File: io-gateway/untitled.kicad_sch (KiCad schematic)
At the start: 6 parts, among them J1 1752201, J2 1752201, J3 1752201, J4 Screw_Terminal_01x09, J5 Screw_Terminal_01x09, J6 Screw_Terminal_01x09

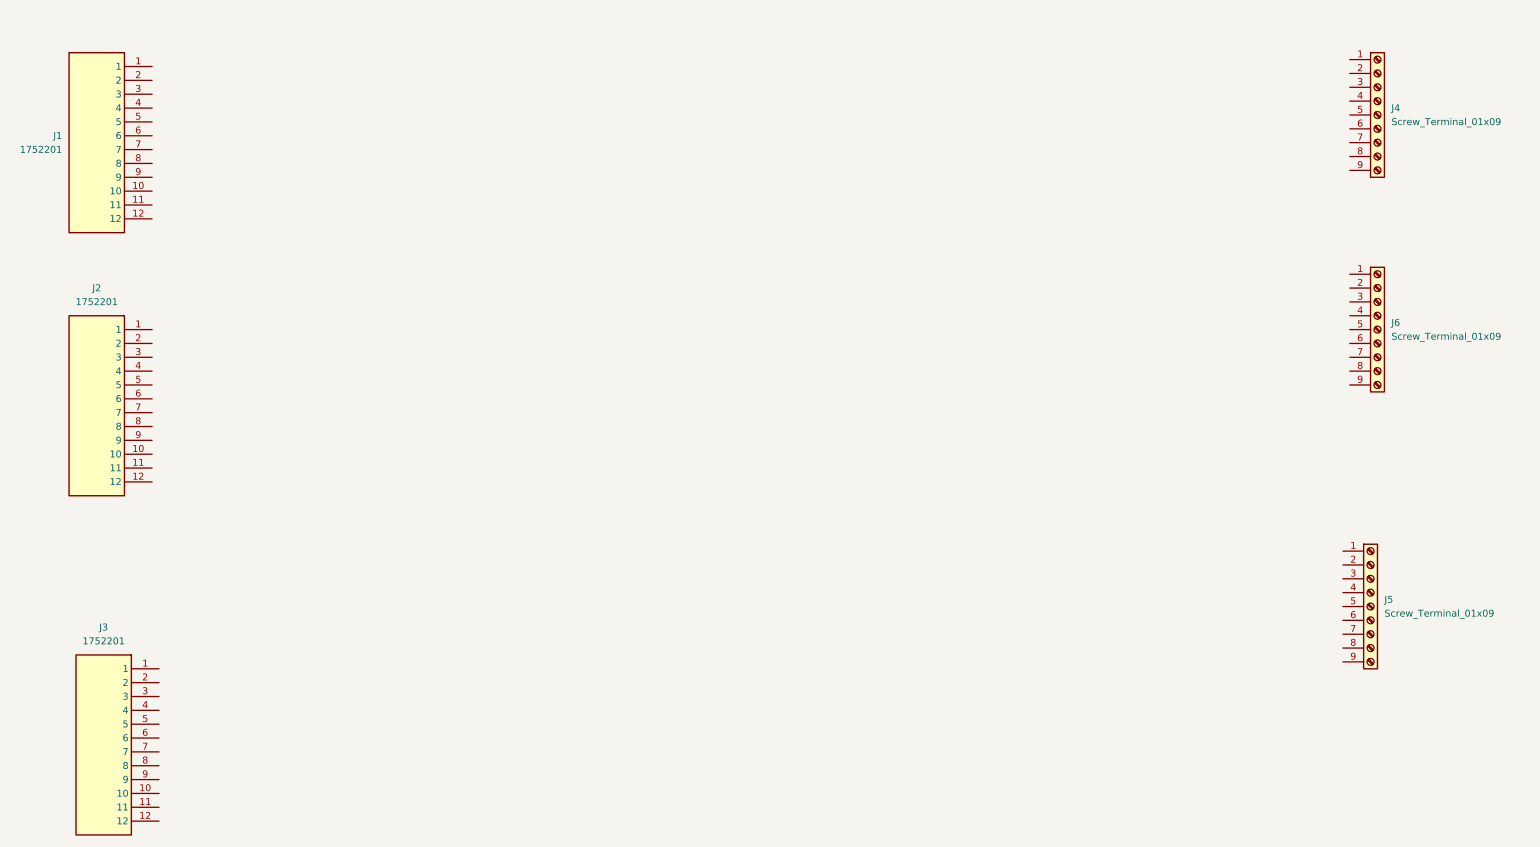
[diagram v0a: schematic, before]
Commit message: Label Terminal Block Pins
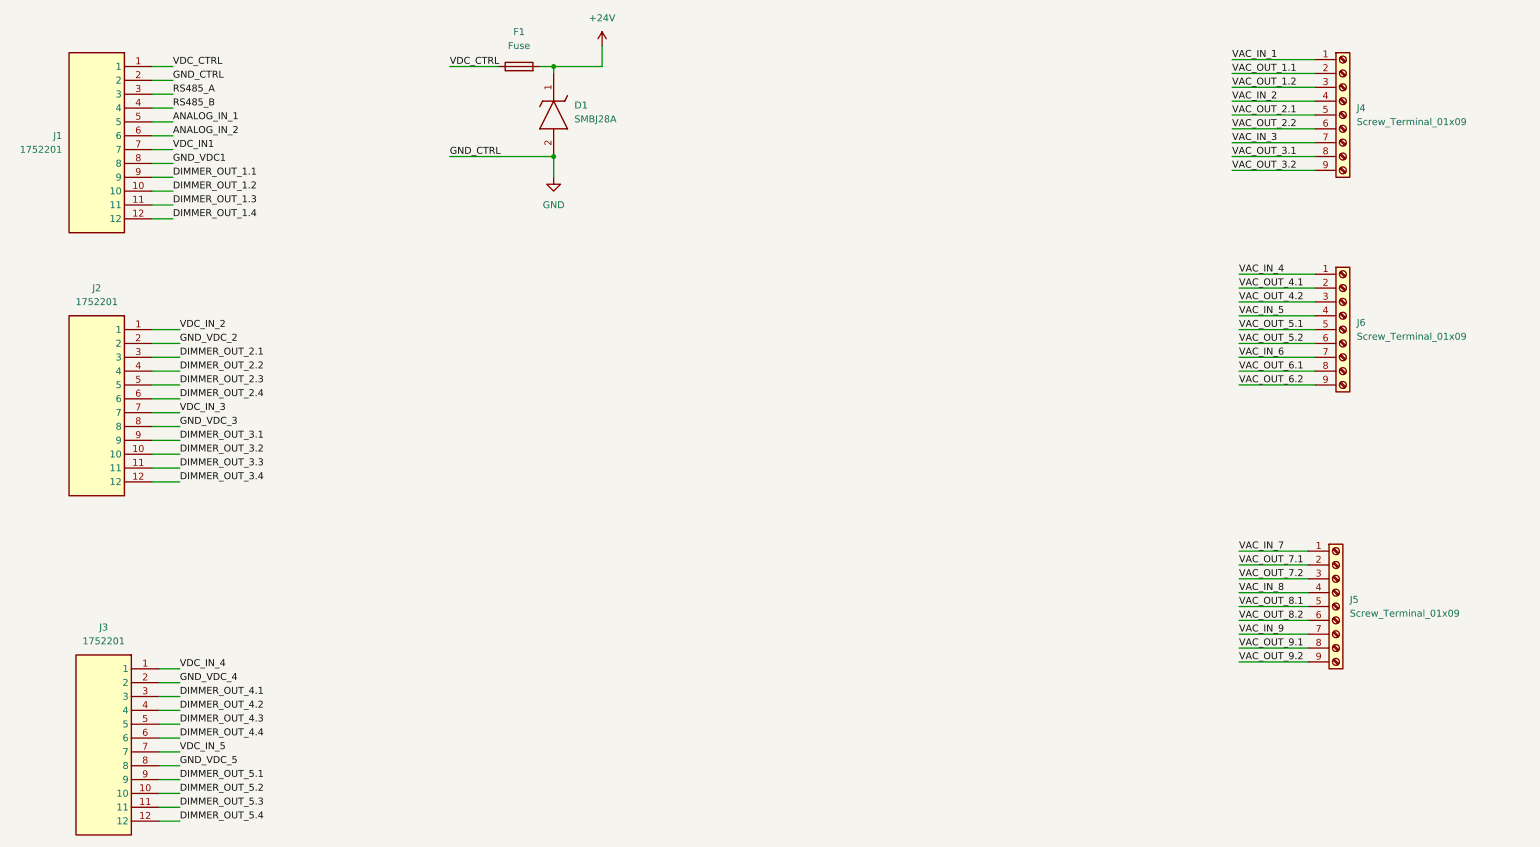
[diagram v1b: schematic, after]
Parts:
- added D1: SMBJ28A, TVS_Diodes:DIOM5436X244N, symbol SMBJ28A:SMBJ28A
- added F1: Fuse, Fuse:Fuseholder_Cylinder-5x20mm_Wuerth_696103101002-SMD_Horizontal_Open, symbol Device:Fuse
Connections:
- net VDC_CTRL: now reaches J1.1
- net VDC_CTRL: now also F1.1
- net DIMMER_OUT_1.2: now reaches J1.10
- net DIMMER_OUT_1.3: now reaches J1.11
- net DIMMER_OUT_1.4: now reaches J1.12
- net GND: now reaches J1.2
- net GND: now also D1.2 (A)
- net RS485_A: now reaches J1.3
- net RS485_B: now reaches J1.4
- net ANALOG_IN_1: now reaches J1.5
- net ANALOG_IN_2: now reaches J1.6
- net VDC_IN1: now reaches J1.7
- net GND_VDC1: now reaches J1.8
- net DIMMER_OUT_1.1: now reaches J1.9
- net VDC_IN_4: now reaches J3.1
- net DIMMER_OUT_5.2: now reaches J3.10
- net DIMMER_OUT_5.3: now reaches J3.11
- net DIMMER_OUT_5.4: now reaches J3.12
- net GND_VDC_4: now reaches J3.2
- net DIMMER_OUT_4.1: now reaches J3.3
- net DIMMER_OUT_4.2: now reaches J3.4
- net DIMMER_OUT_4.3: now reaches J3.5
- net DIMMER_OUT_4.4: now reaches J3.6
- net VDC_IN_5: now reaches J3.7
- net GND_VDC_5: now reaches J3.8
- net DIMMER_OUT_5.1: now reaches J3.9
- net VAC_IN_7: now reaches J5.1 (Pin_1)
- net VAC_OUT_7.1: now reaches J5.2 (Pin_2)
- net VAC_OUT_7.2: now reaches J5.3 (Pin_3)
- net VAC_IN_8: now reaches J5.4 (Pin_4)
- net VAC_OUT_8.1: now reaches J5.5 (Pin_5)
- net VAC_OUT_8.2: now reaches J5.6 (Pin_6)
- net VAC_IN_9: now reaches J5.7 (Pin_7)
- net VAC_OUT_9.1: now reaches J5.8 (Pin_8)
- net VAC_OUT_9.2: now reaches J5.9 (Pin_9)
- net VAC_IN_1: now reaches J4.1 (Pin_1)
- net VAC_OUT_1.1: now reaches J4.2 (Pin_2)
- net VAC_OUT_1.2: now reaches J4.3 (Pin_3)
- net VAC_IN_2: now reaches J4.4 (Pin_4)
- net VAC_OUT_2.1: now reaches J4.5 (Pin_5)
- net VAC_OUT_2.2: now reaches J4.6 (Pin_6)
- net VAC_IN_3: now reaches J4.7 (Pin_7)
- net VAC_OUT_3.1: now reaches J4.8 (Pin_8)
- net VAC_OUT_3.2: now reaches J4.9 (Pin_9)
- net VDC_IN_2: now reaches J2.1
- net DIMMER_OUT_3.2: now reaches J2.10
- net DIMMER_OUT_3.3: now reaches J2.11
- net DIMMER_OUT_3.4: now reaches J2.12
- net GND_VDC_2: now reaches J2.2
- net DIMMER_OUT_2.1: now reaches J2.3
- net DIMMER_OUT_2.2: now reaches J2.4
- net DIMMER_OUT_2.3: now reaches J2.5
- net DIMMER_OUT_2.4: now reaches J2.6
- net VDC_IN_3: now reaches J2.7
- net GND_VDC_3: now reaches J2.8
- net DIMMER_OUT_3.1: now reaches J2.9
- net VAC_IN_4: now reaches J6.1 (Pin_1)
- net VAC_OUT_4.1: now reaches J6.2 (Pin_2)
- net VAC_OUT_4.2: now reaches J6.3 (Pin_3)
- net VAC_IN_5: now reaches J6.4 (Pin_4)
- net VAC_OUT_5.1: now reaches J6.5 (Pin_5)
- net VAC_OUT_5.2: now reaches J6.6 (Pin_6)
- net VAC_IN_6: now reaches J6.7 (Pin_7)
- net VAC_OUT_6.1: now reaches J6.8 (Pin_8)
- net VAC_OUT_6.2: now reaches J6.9 (Pin_9)
- new net +24V: D1.1 (K), F1.2
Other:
- moved on the sheet: J4, J5, J6

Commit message: add relays
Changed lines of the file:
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@@
-	(wire
-		(pts
-			(xy 238.76 27.94) (xy 254 27.94)
-		)
-		(stroke
-			(width 0)
-			(type default)
-		)
-	)
 	(wire
 		(pts
@@
 	(wire
 		(pts
-			(xy 238.76 38.1) (xy 254 38.1)
+			(xy 234.95 30.48) (xy 254 30.48)
 		)
 		(stroke
@@
 	(wire
 		(pts
+			(xy 234.95 33.02) (xy 254 33.02)
+		)
+		(stroke
+			(width 0)
+			(type default)
+		)
+	)
+	(wire
+		(pts
 			(xy 40.64 39.37) (xy 44.45 39.37)
 		)
@@
 	(wire
 		(pts
+			(xy 234.95 40.64) (xy 254 40.64)
+		)
+		(stroke
+			(width 0)
+			(type default)
+		)
+	)
+	(wire
+		(pts
+			(xy 234.95 27.94) (xy 254 27.94)
+		)
+		(stroke
+			(width 0)
+			(type default)
+		)
+	)
+	(wire
+		(pts
 			(xy 41.91 142.24) (xy 45.72 142.24)
 		)
@@
 	(wire
 		(pts
-			(xy 238.76 40.64) (xy 254 40.64)
-		)
-		(stroke
-			(width 0)
-			(type default)
-		)
-	)
-	(wire
-		(pts
 			(xy 40.64 44.45) (xy 44.45 44.45)
 		)
@@
 	(wire
 		(pts
-			(xy 238.76 35.56) (xy 254 35.56)
-		)
-		(stroke
-			(width 0)
-			(type default)
-		)
-	)
-	(wire
-		(pts
 			(xy 40.64 95.25) (xy 45.72 95.25)
 		)
@@
 	(wire
 		(pts
-			(xy 238.76 45.72) (xy 254 45.72)
-		)
-		(stroke
-			(width 0)
-			(type default)
-		)
-	)
-	(wire
-		(pts
 			(xy 240.03 118.11) (xy 252.73 118.11)
 		)
@@
 	(wire
 		(pts
+			(xy 234.95 45.72) (xy 254 45.72)
+		)
+		(stroke
+			(width 0)
+			(type default)
+		)
+	)
+	(wire
+		(pts
 			(xy 41.91 162.56) (xy 45.72 162.56)
 		)
@@
 	(wire
 		(pts
+			(xy 234.95 25.4) (xy 254 25.4)
+		)
+		(stroke
+			(width 0)
+			(type default)
+		)
+	)
+	(wire
+		(pts
 			(xy 240.03 69.85) (xy 254 69.85)
 		)
@@
 	(wire
 		(pts
+			(xy 234.95 38.1) (xy 254 38.1)
+		)
+		(stroke
+			(width 0)
+			(type default)
+		)
+	)
+	(wire
+		(pts
+			(xy 234.95 43.18) (xy 254 43.18)
+		)
+		(stroke
+			(width 0)
+			(type default)
+		)
+	)
+	(wire
+		(pts
 			(xy 240.03 74.93) (xy 254 74.93)
 		)
@@
 	(wire
 		(pts
-			(xy 238.76 25.4) (xy 254 25.4)
-		)
-		(stroke
-			(width 0)
-			(type default)
-		)
-	)
-	(wire
-		(pts
 			(xy 240.03 120.65) (xy 252.73 120.65)
 		)
@@
 	(wire
 		(pts
+			(xy 234.95 35.56) (xy 254 35.56)
+		)
+		(stroke
+			(width 0)
+			(type default)
+		)
+	)
+	(wire
+		(pts
 			(xy 40.64 29.21) (xy 44.45 29.21)
 		)
@@
 	(wire
 		(pts
-			(xy 238.76 30.48) (xy 254 30.48)
-		)
-		(stroke
-			(width 0)
-			(type default)
-		)
-	)
-	(wire
-		(pts
-			(xy 238.76 43.18) (xy 254 43.18)
-		)
-		(stroke
-			(width 0)
-			(type default)
-		)
-	)
-	(wire
-		(pts
 			(xy 123.19 26.67) (xy 114.3 26.67)
 		)
@@
 		(pts
 			(xy 41.91 152.4) (xy 45.72 152.4)
-		)
-		(stroke
-			(width 0)
-			(type default)
-		)
-	)
-	(wire
-		(pts
-			(xy 238.76 33.02) (xy 254 33.02)
 		)
 		(stroke
@@
 		)
 	)
+	(global_label "VAC_OUT_2.2"
+		(shape input)
+		(at 234.95 38.1 180)
+		(fields_autoplaced yes)
+		(effects
+			(font
+				(size 1.27 1.27)
+			)
+			(justify right)
+		)
+		(property "Intersheetrefs" "${INTERSHEET_REFS}"
+			(at 219.93 38.1 0)
+			(effects
+				(font
+					(size 1.27 1.27)
+				)
+				(justify right)
+				(hide yes)
+			)
+		)
+	)
+	(global_label "VAC_OUT_3.1"
+		(shape input)
+		(at 234.95 43.18 180)
+		(fields_autoplaced yes)
+		(effects
+			(font
+				(size 1.27 1.27)
+			)
+			(justify right)
+		)
+		(property "Intersheetrefs" "${INTERSHEET_REFS}"
+			(at 219.93 43.18 0)
+			(effects
+				(font
+					(size 1.27 1.27)
+				)
+				(justify right)
+				(hide yes)
+			)
+		)
+	)
+	(global_label "VAC_IN_2"
+		(shape input)
+		(at 234.95 33.02 180)
+		(fields_autoplaced yes)
+		(effects
+			(font
+				(size 1.27 1.27)
+			)
+			(justify right)
+		)
+		(property "Intersheetrefs" "${INTERSHEET_REFS}"
+			(at 223.4376 33.02 0)
+			(effects
+				(font
+					(size 1.27 1.27)
+				)
+				(justify right)
+				(hide yes)
+			)
+		)
+	)
+	(global_label "VAC_OUT_3.2"
+		(shape input)
+		(at 234.95 45.72 180)
+		(fields_autoplaced yes)
+		(effects
+			(font
+				(size 1.27 1.27)
+			)
+			(justify right)
+		)
+		(property "Intersheetrefs" "${INTERSHEET_REFS}"
+			(at 219.93 45.72 0)
+			(effects
+				(font
+					(size 1.27 1.27)
+				)
+				(justify right)
+				(hide yes)
+			)
+		)
+	)
+	(global_label "VAC_OUT_2.1"
+		(shape input)
+		(at 234.95 35.56 180)
+		(fields_autoplaced yes)
+		(effects
+			(font
+				(size 1.27 1.27)
+			)
+			(justify right)
+		)
+		(property "Intersheetrefs" "${INTERSHEET_REFS}"
+			(at 219.93 35.56 0)
+			(effects
+				(font
+					(size 1.27 1.27)
+				)
+				(justify right)
+				(hide yes)
+			)
+		)
+	)
+	(global_label "VAC_IN_3"
+		(shape input)
+		(at 234.95 40.64 180)
+		(fields_autoplaced yes)
+		(effects
+			(font
+				(size 1.27 1.27)
+			)
+			(justify right)
+		)
+		(property "Intersheetrefs" "${INTERSHEET_REFS}"
+			(at 223.4376 40.64 0)
+			(effects
+				(font
+					(size 1.27 1.27)
+				)
+				(justify right)
+				(hide yes)
+			)
+		)
+	)
+	(global_label "VAC_OUT_1.2"
+		(shape input)
+		(at 234.95 30.48 180)
+		(fields_autoplaced yes)
+		(effects
+			(font
+				(size 1.27 1.27)
+			)
+			(justify right)
+		)
+		(property "Intersheetrefs" "${INTERSHEET_REFS}"
+			(at 219.93 30.48 0)
+			(effects
+				(font
+					(size 1.27 1.27)
+				)
+				(justify right)
+				(hide yes)
+			)
+		)
+	)
+	(global_label "VAC_OUT_1.1"
+		(shape input)
+		(at 234.95 27.94 180)
+		(fields_autoplaced yes)
+		(effects
+			(font
+				(size 1.27 1.27)
+			)
+			(justify right)
+		)
+		(property "Intersheetrefs" "${INTERSHEET_REFS}"
+			(at 219.93 27.94 0)
+			(effects
+				(font
+					(size 1.27 1.27)
+				)
+				(justify right)
+				(hide yes)
+			)
+		)
+	)
+	(global_label "VAC_IN_1"
+		(shape input)
+		(at 234.95 25.4 180)
+		(fields_autoplaced yes)
+		(effects
+			(font
+				(size 1.27 1.27)
+			)
+			(justify right)
+		)
+		(property "Intersheetrefs" "${INTERSHEET_REFS}"
+			(at 223.4376 25.4 0)
+			(effects
+				(font
+					(size 1.27 1.27)
+				)
+				(justify right)
+				(hide yes)
+			)
+		)
+	)

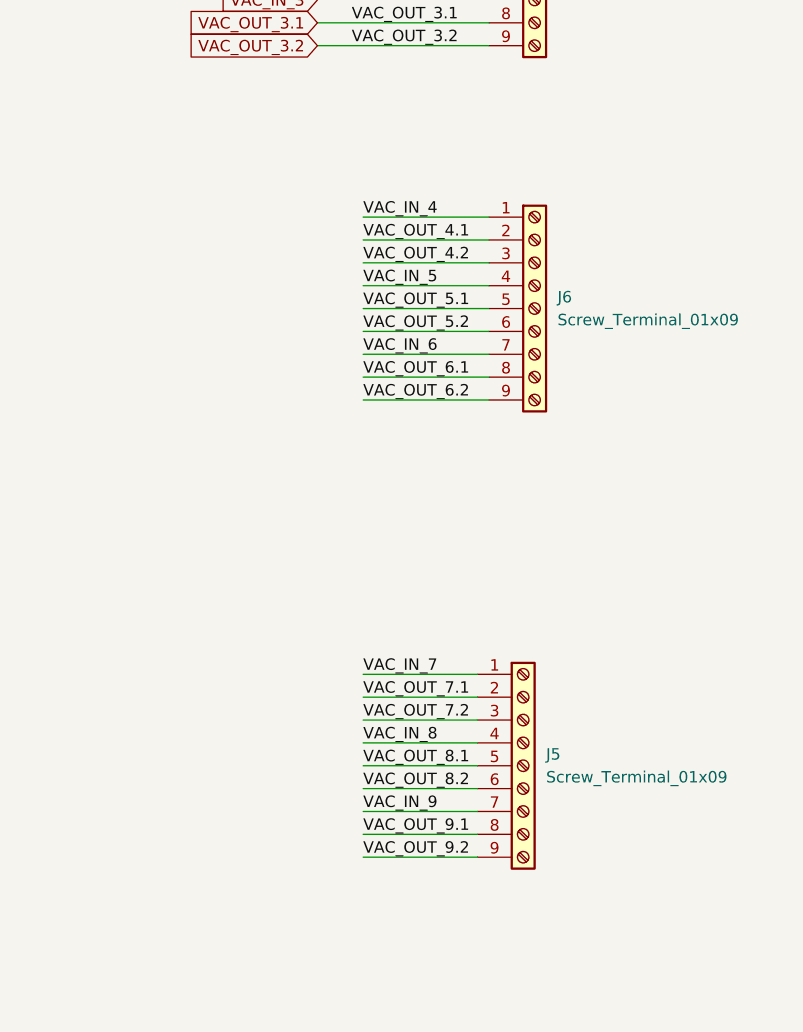
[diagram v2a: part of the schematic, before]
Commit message: Place Relays
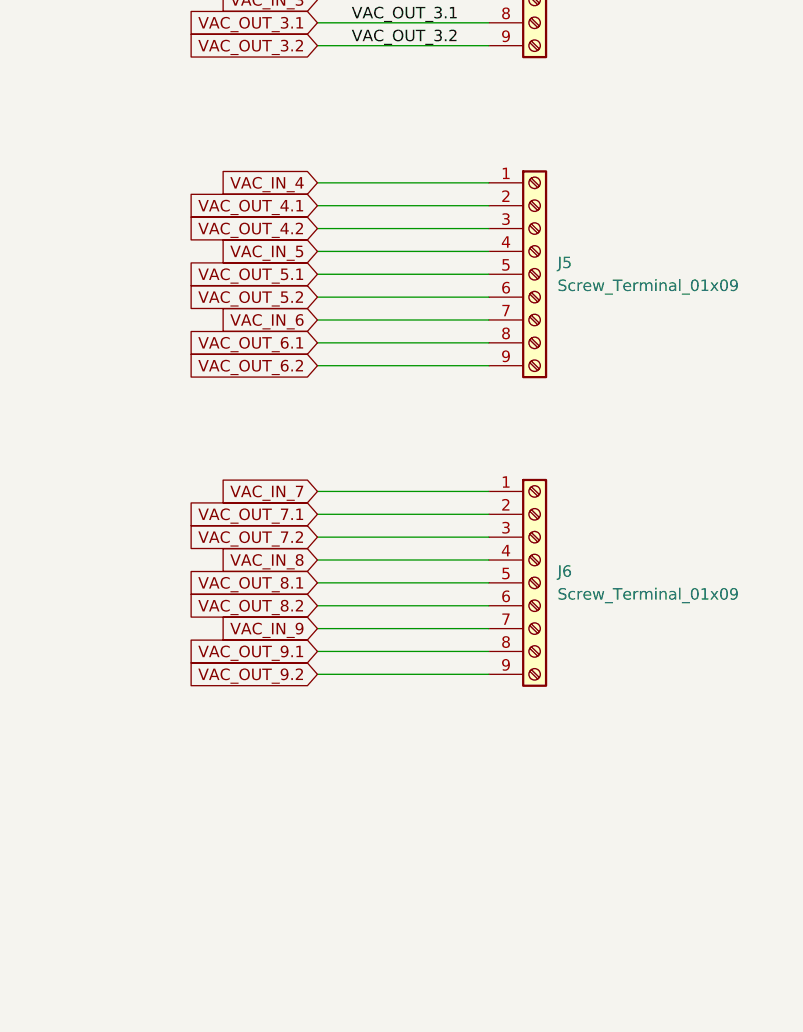
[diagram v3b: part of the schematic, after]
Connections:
- net VAC_IN_4: now also J5.1 (Pin_1); no longer J6.1 (Pin_1)
- net VAC_IN_5: now also J5.4 (Pin_4); no longer J6.4 (Pin_4)
- net VAC_IN_6: now also J5.7 (Pin_7); no longer J6.7 (Pin_7)
- net VAC_IN_7: now also J6.1 (Pin_1); no longer J5.1 (Pin_1)
- net VAC_IN_8: now also J6.4 (Pin_4); no longer J5.4 (Pin_4)
- net VAC_IN_9: now also J6.7 (Pin_7); no longer J5.7 (Pin_7)
- net VAC_OUT_4.1: now also J5.2 (Pin_2); no longer J6.2 (Pin_2)
- net VAC_OUT_4.2: now also J5.3 (Pin_3); no longer J6.3 (Pin_3)
- net VAC_OUT_5.1: now also J5.5 (Pin_5); no longer J6.5 (Pin_5)
- net VAC_OUT_5.2: now also J5.6 (Pin_6); no longer J6.6 (Pin_6)
- net VAC_OUT_6.1: now also J5.8 (Pin_8); no longer J6.8 (Pin_8)
- net VAC_OUT_6.2: now also J5.9 (Pin_9); no longer J6.9 (Pin_9)
- net VAC_OUT_7.1: now also J6.2 (Pin_2); no longer J5.2 (Pin_2)
- net VAC_OUT_7.2: now also J6.3 (Pin_3); no longer J5.3 (Pin_3)
- net VAC_OUT_8.1: now also J6.5 (Pin_5); no longer J5.5 (Pin_5)
- net VAC_OUT_8.2: now also J6.6 (Pin_6); no longer J5.6 (Pin_6)
- net VAC_OUT_9.1: now also J6.8 (Pin_8); no longer J5.8 (Pin_8)
- net VAC_OUT_9.2: now also J6.9 (Pin_9); no longer J5.9 (Pin_9)
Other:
- moved on the sheet: J5, J6

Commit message: update
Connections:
- net GND_VDC_4 is gone; now on net GND_DIM3: J3.2
- net GND_VDC_5 is gone; now on net GND_DIM5: J3.8
- net VDC_IN_4 is gone; now on net VIN_DIM3: J3.1
- net VDC_IN_5 is gone; now on net VIN_DIM5: J3.7
- net DIMMER_OUT_1.1 renamed DIM1_VLED+
- net DIMMER_OUT_1.2 renamed DIM1_VLED-
- net DIMMER_OUT_1.3 renamed DIM2_VLED+
- net DIMMER_OUT_1.4 renamed DIM2_VLED-
- net DIMMER_OUT_2.1 renamed DIM3_VLED+
- net DIMMER_OUT_2.2 renamed DIM3_VLED-
- net DIMMER_OUT_2.3 renamed DIM4_VLED+
- net DIMMER_OUT_2.4 renamed DIM4_VLED-
- net DIMMER_OUT_3.1 renamed DIM5_VLED+
- net DIMMER_OUT_3.2 renamed DIM5_VLED-
- net DIMMER_OUT_3.3 renamed DIM6_VLED+
- net DIMMER_OUT_3.4 renamed DIM6_VLED-
- net DIMMER_OUT_4.1 renamed DIM7_VLED+
- net DIMMER_OUT_4.2 renamed DIM7_VLED-
- net DIMMER_OUT_4.3 renamed DIM8_VLED+
- net DIMMER_OUT_4.4 renamed DIM8_VLED-
- net DIMMER_OUT_5.1 renamed DIM9_VLED+
- net DIMMER_OUT_5.2 renamed DIM9_VLED-
- net DIMMER_OUT_5.3 renamed DIM10_VLED+
- net DIMMER_OUT_5.4 renamed DIM10_VLED-
- net GND_VDC1 renamed GND_DIM1
- net GND_VDC_2 renamed GND_DIM3
- net GND_VDC_3 renamed GND_DIM5
- net VDC_IN1 renamed VIN_DIM1
- net VDC_IN_2 renamed VIN_DIM3
- net VDC_IN_3 renamed VIN_DIM5
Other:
- moved on the sheet: J2

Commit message: layout for first dimmer
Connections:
- net DIM10_VLED+ renamed DIM10_VLED_VCC
- net DIM10_VLED- renamed DIM10_VLED_GND
- net DIM1_VLED+ renamed DIM1_VLED_VCC
- net DIM1_VLED- renamed DIM1_VLED_GND
- net DIM2_VLED+ renamed DIM2_VLED_VCC
- net DIM2_VLED- renamed DIM2_VLED_GND
- net DIM3_VLED+ renamed DIM3_VLED_VCC
- net DIM3_VLED- renamed DIM3_VLED_GND
- net DIM4_VLED+ renamed DIM4_VLED_VCC
- net DIM4_VLED- renamed DIM4_VLED_GND
- net DIM5_VLED+ renamed DIM5_VLED_VCC
- net DIM5_VLED- renamed DIM5_VLED_GND
- net DIM6_VLED+ renamed DIM6_VLED_VCC
- net DIM6_VLED- renamed DIM6_VLED_GND
- net DIM7_VLED+ renamed DIM7_VLED_VCC
- net DIM7_VLED- renamed DIM7_VLED_GND
- net DIM8_VLED+ renamed DIM8_VLED_VCC
- net DIM8_VLED- renamed DIM8_VLED_GND
- net DIM9_VLED+ renamed DIM9_VLED_VCC
- net DIM9_VLED- renamed DIM9_VLED_GND
- net VAC_OUT_1.1 renamed VAC_OUT_1
- net VAC_OUT_1.2: no longer names the net of J4.3 (Pin_3)
- net VAC_OUT_2.1 renamed VAC_OUT_2
- net VAC_OUT_2.2: no longer names the net of J4.6 (Pin_6)
- net VAC_OUT_3.1 renamed VAC_OUT_3
- net VAC_OUT_3.2: no longer names the net of J4.9 (Pin_9)
- net VAC_OUT_4.1 renamed VAC_OUT_4
- net VAC_OUT_4.2: no longer names the net of J5.3 (Pin_3)
- net VAC_OUT_5.1 renamed VAC_OUT_5
- net VAC_OUT_5.2: no longer names the net of J5.6 (Pin_6)
- net VAC_OUT_6.1 renamed VAC_OUT_6
- net VAC_OUT_6.2: no longer names the net of J5.9 (Pin_9)
- net VAC_OUT_7.1 renamed VAC_OUT_7
- net VAC_OUT_7.2: no longer names the net of J6.3 (Pin_3)
- net VAC_OUT_8.1 renamed VAC_OUT_8
- net VAC_OUT_8.2: no longer names the net of J6.6 (Pin_6)
- net VAC_OUT_9.1 renamed VAC_OUT_9
- net VAC_OUT_9.2: no longer names the net of J6.9 (Pin_9)

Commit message: upd
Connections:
- net GND_DIM1 is gone; now on net GND: J1.8
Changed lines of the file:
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@@
 		(color 0 0 0 0)
 	)
+	(junction
+		(at 114.3 44.45)
+		(diameter 0)
+		(color 0 0 0 0)
+	)
 	(wire
 		(pts
@@
 	(wire
 		(pts
+			(xy 114.3 44.45) (xy 114.3 46.99)
+		)
+		(stroke
+			(width 0)
+			(type default)
+		)
+	)
+	(wire
+		(pts
 			(xy 40.64 90.17) (xy 67.31 90.17)
 		)
@@
 	(wire
 		(pts
-			(xy 40.64 44.45) (xy 67.31 44.45)
+			(xy 40.64 44.45) (xy 114.3 44.45)
 		)
 		(stroke
@@
 	(wire
 		(pts
-			(xy 114.3 43.18) (xy 114.3 46.99)
-		)
-		(stroke
+			(xy 114.3 43.18) (xy 114.3 44.45)
+		)
+		(stroke

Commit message: temp
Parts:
- removed D1: SMBJ28A, TVS_Diodes:DIOM5436X244N, symbol SMBJ28A:SMBJ28A
- removed F1: Fuse, Fuse:Fuseholder_Cylinder-5x20mm_Wuerth_696103101002-SMD_Horizontal_Open, symbol Device:Fuse
- removed J1, J2, J3: 1752201, TerminalBlock_Phoenix:1752201, symbol 1752201:1752201
- removed J4, J5, J6: Screw_Terminal_01x09, TerminalBlock_TE-Connectivity:TerminalBlock_TE_282836-9_1x09_P5mm_Horizontal, symbol Connector:Screw_Terminal_01x09
